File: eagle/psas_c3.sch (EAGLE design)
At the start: 27 parts, among them IC1 CP210X_USB_UART, U1 MIC5219 3.3V, Y1 32MHz

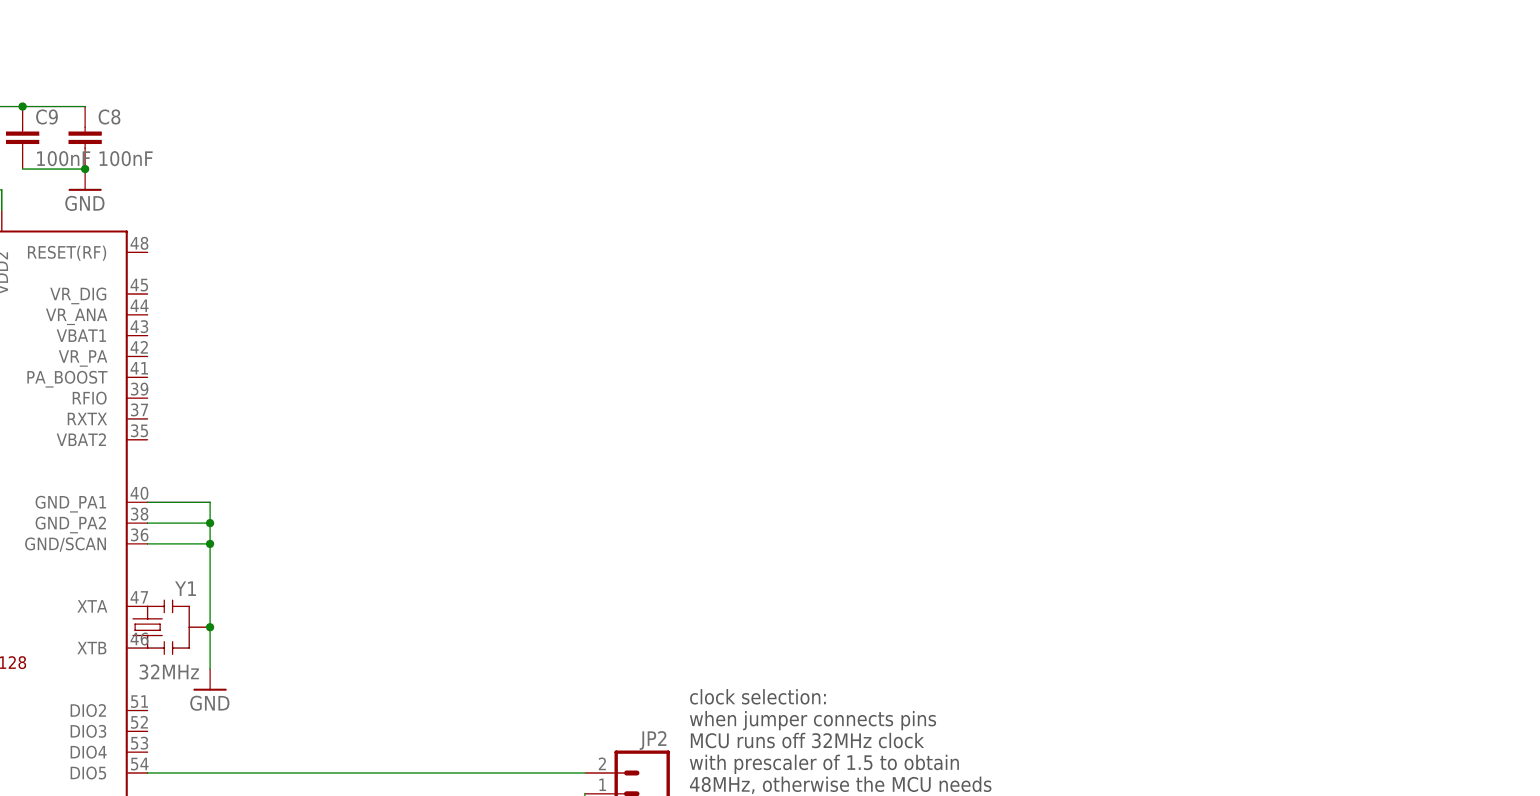
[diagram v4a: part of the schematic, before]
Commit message: Updated schematic with RF parts, need to do values
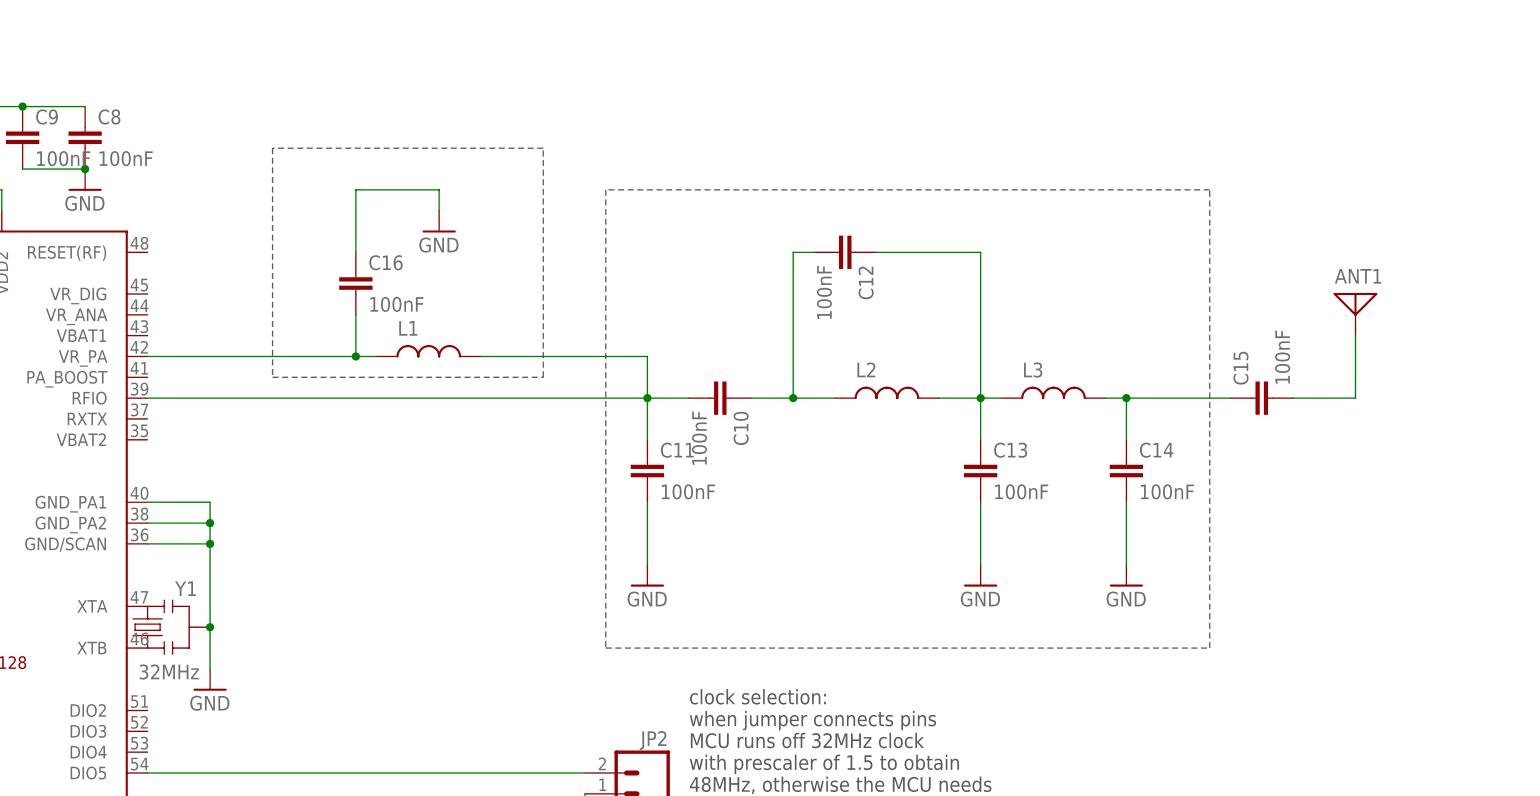
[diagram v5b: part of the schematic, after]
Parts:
- added ANT1: (no value), discrete:ANTENNA
- added C10, C11, C12, C13, C14, C15, C16: 100nF, rcl_custom:C-EU0603-B-NOSILK
- added L1, L2, L3: (no value), rcl_custom:L-US0603-B-NOSILK
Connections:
- new net N$16: C10.2, C11.1, L1.2, U$1.RFIO
- new net N$17: C12.1, C13.1, L2.2, L3.1
- new net N$18: C10.1, C12.2, L2.1
- new net N$19: ANT1.1, C15.2
- new net N$20: C16.2, L1.1, U$1.VR_PA
- new net N$21: C14.1, C15.1, L3.2
- net GND: now also C11.2, C13.2, C14.2, C16.1
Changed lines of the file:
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@@
 <?xml version="1.0" encoding="utf-8"?>
 <!DOCTYPE eagle SYSTEM "eagle.dtd">
-<eagle version="7.3.0">
+<eagle version="6.3">
 <drawing>
 <settings>
@@
 </part>
 <part name="JP2" library="SparkFun-v5" deviceset="M02" device="PTH"/>
+<part name="C10" library="rcl_custom" deviceset="C-EU" device="0603-B-NOSILK" value="100nF"/>
+<part name="C11" library="rcl_custom" deviceset="C-EU" device="0603-B-NOSILK" value="100nF"/>
+<part name="C12" library="rcl_custom" deviceset="C-EU" device="0603-B-NOSILK" value="100nF"/>
+<part name="C13" library="rcl_custom" deviceset="C-EU" device="0603-B-NOSILK" value="100nF"/>
+<part name="C14" library="rcl_custom" deviceset="C-EU" device="0603-B-NOSILK" value="100nF"/>
+<part name="GND17" library="Vibrogait_prototype" deviceset="GND" device=""/>
+<part name="GND18" library="Vibrogait_prototype" deviceset="GND" device=""/>
+<part name="GND19" library="Vibrogait_prototype" deviceset="GND" device=""/>
+<part name="C15" library="rcl_custom" deviceset="C-EU" device="0603-B-NOSILK" value="100nF"/>
+<part name="C16" library="rcl_custom" deviceset="C-EU" device="0603-B-NOSILK" value="100nF"/>
+<part name="GND20" library="Vibrogait_prototype" deviceset="GND" device=""/>
+<part name="ANT1" library="discrete" deviceset="ANTENNA" device=""/>
+<part name="L1" library="rcl_custom" deviceset="L-US" device="0603-B-NOSILK"/>
+<part name="L2" library="rcl_custom" deviceset="L-US" device="0603-B-NOSILK"/>
+<part name="L3" library="rcl_custom" deviceset="L-US" device="0603-B-NOSILK"/>
 </parts>
 <sheets>
@@
 to run off internal clock reference
 (see datasheet for details)</text>
+<wire x1="127" y1="134.62" x2="127" y2="106.68" width="0.1524" layer="97" style="dashdot"/>
+<wire x1="127" y1="106.68" x2="160.02" y2="106.68" width="0.1524" layer="97" style="dashdot"/>
+<wire x1="160.02" y1="106.68" x2="160.02" y2="134.62" width="0.1524" layer="97" style="dashdot"/>
+<wire x1="160.02" y1="134.62" x2="127" y2="134.62" width="0.1524" layer="97" style="dashdot"/>
+<wire x1="167.64" y1="129.54" x2="167.64" y2="73.66" width="0.1524" layer="97" style="dashdot"/>
+<wire x1="167.64" y1="73.66" x2="241.3" y2="73.66" width="0.1524" layer="97" style="dashdot"/>
+<wire x1="241.3" y1="73.66" x2="241.3" y2="129.54" width="0.1524" layer="97" style="dashdot"/>
+<wire x1="241.3" y1="129.54" x2="167.64" y2="129.54" width="0.1524" layer="97" style="dashdot"/>
 </plain>
 <instances>
@@
 </instance>
 <instance part="JP2" gate="G$1" x="172.72" y="55.88" rot="MR0"/>
+<instance part="C10" gate="CE" x="182.88" y="104.14" rot="R270"/>
+<instance part="C11" gate="CE" x="172.72" y="96.52"/>
+<instance part="C12" gate="CE" x="198.12" y="121.92" rot="R270"/>
+<instance part="C13" gate="CE" x="213.36" y="96.52"/>
+<instance part="C14" gate="CE" x="231.14" y="96.52"/>
+<instance part="GND17" gate="1" x="172.72" y="81.28"/>
+<instance part="GND18" gate="1" x="231.14" y="81.28"/>
+<instance part="GND19" gate="1" x="213.36" y="81.28"/>
+<instance part="C15" gate="CE" x="246.38" y="104.14" rot="R90"/>
+<instance part="C16" gate="CE" x="137.16" y="119.38"/>
+<instance part="GND20" gate="1" x="147.32" y="124.46"/>
+<instance part="ANT1" gate="A" x="259.08" y="116.84"/>
+<instance part="L1" gate="L" x="147.32" y="109.22"/>
+<instance part="L2" gate="L" x="203.2" y="104.14"/>
+<instance part="L3" gate="L" x="223.52" y="104.14"/>
 </instances>
 <busses>
@@
 <pinref part="GND16" gate="1" pin="GND"/>
 <wire x1="365.76" y1="226.06" x2="365.76" y2="233.68" width="0.1524" layer="91"/>
+</segment>
+<segment>
+<pinref part="C11" gate="CE" pin="2"/>
+<pinref part="GND17" gate="1" pin="GND"/>
+<wire x1="172.72" y1="91.44" x2="172.72" y2="83.82" width="0.1524" layer="91"/>
+</segment>
+<segment>
+<pinref part="C13" gate="CE" pin="2"/>
+<pinref part="GND19" gate="1" pin="GND"/>
+<wire x1="213.36" y1="91.44" x2="213.36" y2="83.82" width="0.1524" layer="91"/>
+</segment>
+<segment>
+<pinref part="C14" gate="CE" pin="2"/>
+<pinref part="GND18" gate="1" pin="GND"/>
+<wire x1="231.14" y1="91.44" x2="231.14" y2="83.82" width="0.1524" layer="91"/>
+</segment>
+<segment>
+<pinref part="C16" gate="CE" pin="1"/>
+<wire x1="137.16" y1="121.92" x2="137.16" y2="129.54" width="0.1524" layer="91"/>
+<wire x1="137.16" y1="129.54" x2="147.32" y2="129.54" width="0.1524" layer="91"/>
+<pinref part="GND20" gate="1" pin="GND"/>
+<wire x1="147.32" y1="129.54" x2="147.32" y2="127" width="0.1524" layer="91"/>
 </segment>
 </net>
@@
 </segment>
 </net>
+<net name="N$16" class="0">
+<segment>
+<pinref part="U$1" gate="G$1" pin="RFIO"/>
+<pinref part="C10" gate="CE" pin="2"/>
+<wire x1="111.76" y1="104.14" x2="172.72" y2="104.14" width="0.1524" layer="91"/>
+<pinref part="C11" gate="CE" pin="1"/>
+<wire x1="172.72" y1="104.14" x2="177.8" y2="104.14" width="0.1524" layer="91"/>
+<wire x1="172.72" y1="99.06" x2="172.72" y2="104.14" width="0.1524" layer="91"/>
+<junction x="172.72" y="104.14"/>
+<pinref part="L1" gate="L" pin="2"/>
+<wire x1="152.4" y1="109.22" x2="172.72" y2="109.22" width="0.1524" layer="91"/>
+<wire x1="172.72" y1="109.22" x2="172.72" y2="104.14" width="0.1524" layer="91"/>
+</segment>
+</net>
+<net name="N$17" class="0">
+<segment>
+<pinref part="C13" gate="CE" pin="1"/>
+<wire x1="213.36" y1="99.06" x2="213.36" y2="104.14" width="0.1524" layer="91"/>
+<junction x="213.36" y="104.14"/>
+<pinref part="C12" gate="CE" pin="1"/>
+<wire x1="200.66" y1="121.92" x2="213.36" y2="121.92" width="0.1524" layer="91"/>
+<wire x1="213.36" y1="121.92" x2="213.36" y2="104.14" width="0.1524" layer="91"/>
+<pinref part="L2" gate="L" pin="2"/>
+<wire x1="208.28" y1="104.14" x2="213.36" y2="104.14" width="0.1524" layer="91"/>
+<pinref part="L3" gate="L" pin="1"/>
+<wire x1="213.36" y1="104.14" x2="215.9" y2="104.14" width="0.1524" layer="91"/>
+</segment>
+</net>
+<net name="N$18" class="0">
+<segment>
+<pinref part="C10" gate="CE" pin="1"/>
+<wire x1="185.42" y1="104.14" x2="190.5" y2="104.14" width="0.1524" layer="91"/>
+<pinref part="C12" gate="CE" pin="2"/>
+<wire x1="193.04" y1="121.92" x2="190.5" y2="121.92" width="0.1524" layer="91"/>
+<wire x1="190.5" y1="121.92" x2="190.5" y2="104.14" width="0.1524" layer="91"/>
+<pinref part="L2" gate="L" pin="1"/>
+<wire x1="190.5" y1="104.14" x2="195.58" y2="104.14" width="0.1524" layer="91"/>
+<junction x="190.5" y="104.14"/>
+</segment>
+</net>
+<net name="N$19" class="0">
+<segment>
+<pinref part="C15" gate="CE" pin="2"/>
+<wire x1="251.46" y1="104.14" x2="259.08" y2="104.14" width="0.1524" layer="91"/>
+<wire x1="259.08" y1="104.14" x2="259.08" y2="111.76" width="0.1524" layer="91"/>
+<pinref part="ANT1" gate="A" pin="1"/>
+</segment>
+</net>
+<net name="N$20" class="0">
+<segment>
+<pinref part="U$1" gate="G$1" pin="VR_PA"/>
+<wire x1="111.76" y1="109.22" x2="137.16" y2="109.22" width="0.1524" layer="91"/>
+<pinref part="C16" gate="CE" pin="2"/>
+<wire x1="137.16" y1="109.22" x2="137.16" y2="114.3" width="0.1524" layer="91"/>
+<pinref part="L1" gate="L" pin="1"/>
+<wire x1="137.16" y1="109.22" x2="139.7" y2="109.22" width="0.1524" layer="91"/>
+<junction x="137.16" y="109.22"/>
+</segment>
+</net>
+<net name="N$21" class="0">
+<segment>
+<pinref part="C14" gate="CE" pin="1"/>
+<pinref part="C15" gate="CE" pin="1"/>
+<wire x1="231.14" y1="104.14" x2="243.84" y2="104.14" width="0.1524" layer="91"/>
+<wire x1="231.14" y1="104.14" x2="231.14" y2="99.06" width="0.1524" layer="91"/>
+<pinref part="L3" gate="L" pin="2"/>
+<wire x1="228.6" y1="104.14" x2="231.14" y2="104.14" width="0.1524" layer="91"/>
+<junction x="231.14" y="104.14"/>
+</segment>
+</net>
